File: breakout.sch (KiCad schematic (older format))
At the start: 16 parts, among them CON1 SD_Card, CON2 USB-MINI-B, P2 CONN_01X40, P3 CONN_01X40, P4 CONN_01X40, P5 A-DF-09-A/KG-T4S

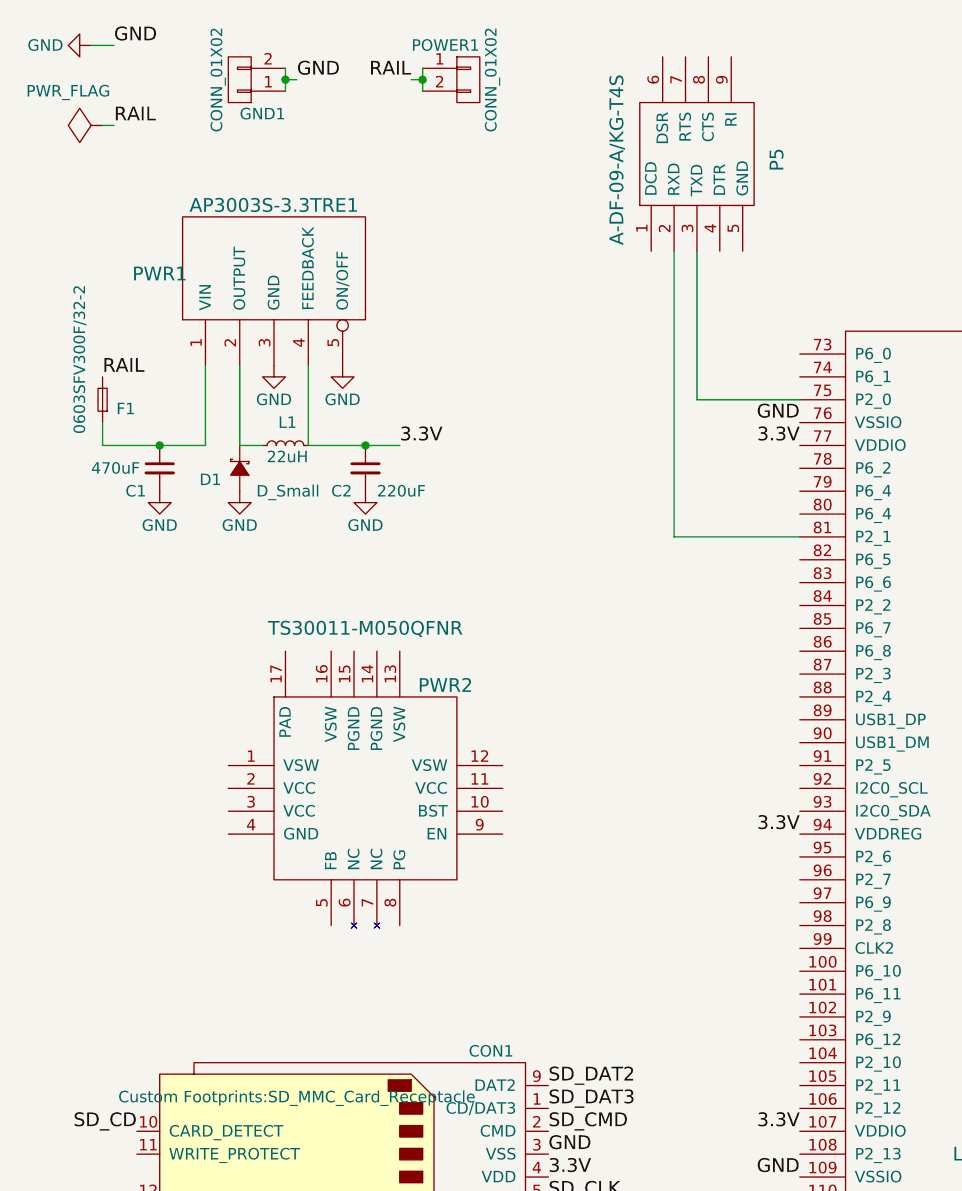
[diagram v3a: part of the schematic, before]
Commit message: added USB_MINI_AB_SMD footprint
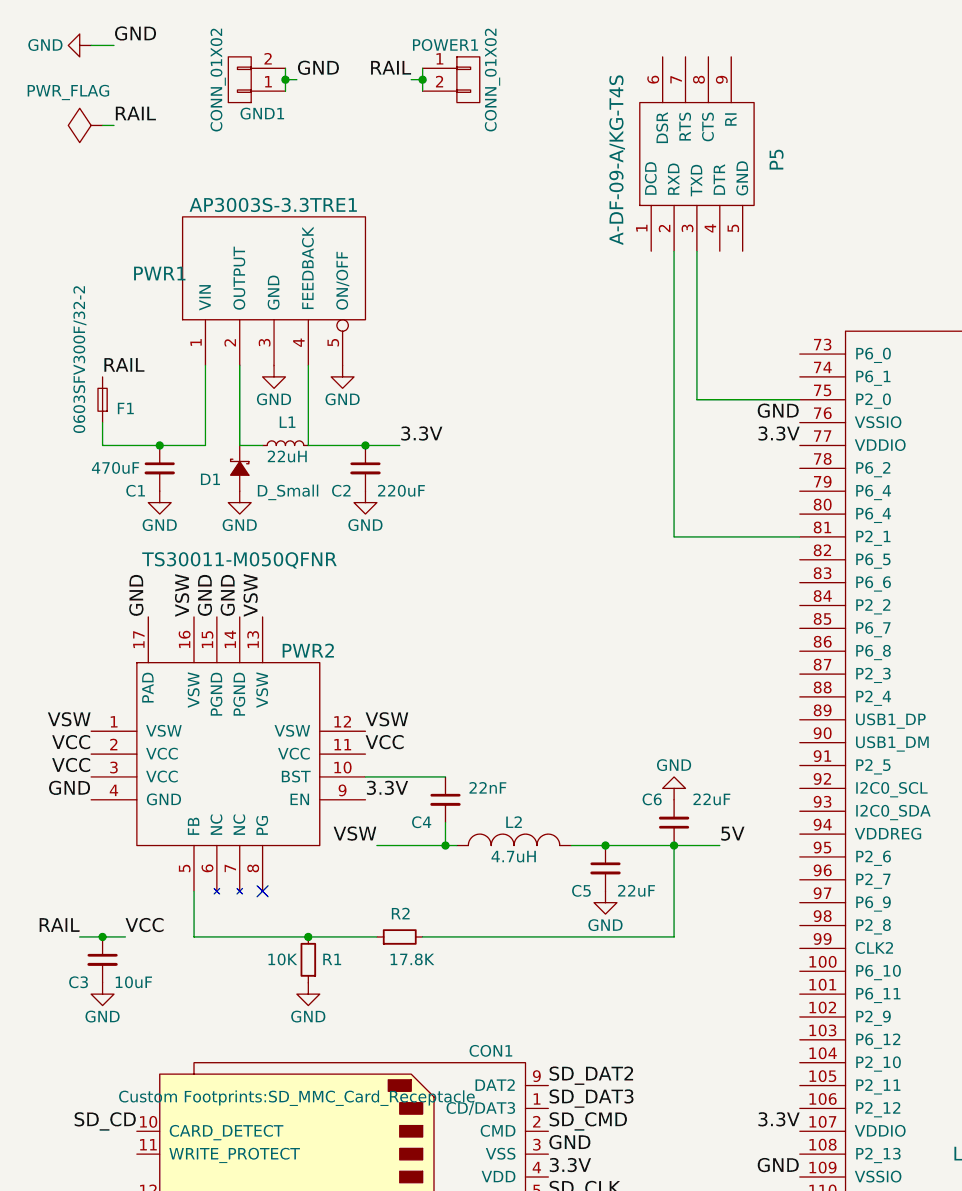
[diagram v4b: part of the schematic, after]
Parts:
- added C3: 10uF, Capacitors_SMD:C_0402, symbol C_Small
- added C4: 22nF, Capacitors_SMD:C_0402, symbol C_Small
- added C5, C6: 22uF, Capacitors_SMD:C_0402, symbol C_Small
- added L2: 4.7uH, Capacitors_SMD:C_0201, symbol INDUCTOR_SMALL
- added R1: 10K, Resistors_SMD:R_0201, symbol R_Small
- added R2: 17.8K, Resistors_SMD:R_0201, symbol R_Small
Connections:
- net 3.3V: now also PWR2.9 (EN); no longer CPU1.94 (VDDREG)
- net GND: now also PWR2.14 (PGND), PWR2.15 (PGND), PWR2.17 (PAD), PWR2.4 (GND), C3.2, C5.2, C6.2, R1.1
- net RAIL: now also PWR2.11 (VCC), PWR2.2 (VCC), PWR2.3 (VCC), C3.1
- net VSW: now reaches PWR2.1 (VSW)
- net VSW: now also PWR2.12 (VSW), PWR2.13 (VSW), PWR2.16 (VSW), C4.2, L2.1
- net at PWR2.10 (BST): now also C4.1
- net at PWR2.5 (FB): now also R1.2, R2.1
- new net 5V: C5.1, C6.1, L2.2, R2.2
- no-connect marks 0 -> 1
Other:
- moved on the sheet: PWR2
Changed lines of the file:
@@
 L TS30011-M050QFNR PWR2
 U 1 1 561BCBF8
-P 2000 3150
-F 0 "PWR2" H 2350 2900 60  0000 C CNN
-F 1 "TS30011-M050QFNR" H 2000 3150 60  0000 C CNN
-F 2 "Housings_DFN_QFN:QFN-16-1EP_3x3mm_Pitch0.5mm" H 2000 3150 60  0001 C CNN
-F 3 "" H 2000 3150 60  0000 C CNN
-	1    2000 3150
-	1    0    0    -1
-$EndComp
-$Comp
-L PWR_FLAG #FLG01
+P 1400 3000
+F 0 "PWR2" H 1750 2750 60  0000 C CNN
+F 1 "TS30011-M050QFNR" H 1450 3150 60  0000 C CNN
+F 2 "Housings_DFN_QFN:QFN-16-1EP_3x3mm_Pitch0.5mm" H 1400 3000 60  0001 C CNN
+F 3 "" H 1400 3000 60  0000 C CNN
+	1    1400 3000
+	1    0    0    -1
+$EndComp
+$Comp
+L PWR_FLAG #FLG1
 U 1 1 561BDFAD
 P 850 950
-F 0 "#FLG01" H 850 1045 50  0001 C CNN
+F 0 "#FLG1" H 850 1045 50  0001 C CNN
 F 1 "PWR_FLAG" V 1000 1100 50  0000 C CNN
 F 2 "" H 850 950 60  0000 C CNN
@@
 RAIL
 $Comp
-L GND #PWR02
+L GND #PWR1
 U 1 1 561BE928
 P 800 600
-F 0 "#PWR02" H 800 350 50  0001 C CNN
+F 0 "#PWR1" H 800 350 50  0001 C CNN
 F 1 "GND" V 800 400 50  0000 C CNN
 F 2 "" H 800 600 60  0000 C CNN
@@
 $EndComp
 $Comp
-L GND #PWR03
+L GND #PWR5
 U 1 1 561C5C16
 P 1600 2000
-F 0 "#PWR03" H 1600 1750 50  0001 C CNN
+F 0 "#PWR5" H 1600 1750 50  0001 C CNN
 F 1 "GND" H 1600 1850 50  0000 C CNN
 F 2 "" H 1600 2000 60  0000 C CNN
@@
 $EndComp
 $Comp
-L GND #PWR04
+L GND #PWR3
 U 1 1 561C5DB0
 P 1100 2550
-F 0 "#PWR04" H 1100 2300 50  0001 C CNN
+F 0 "#PWR3" H 1100 2300 50  0001 C CNN
 F 1 "GND" H 1100 2400 50  0000 C CNN
 F 2 "" H 1100 2550 60  0000 C CNN
@@
 $EndComp
 $Comp
-L GND #PWR05
+L GND #PWR7
 U 1 1 561C5E4C
 P 1900 2000
-F 0 "#PWR05" H 1900 1750 50  0001 C CNN
+F 0 "#PWR7" H 1900 1750 50  0001 C CNN
 F 1 "GND" H 1900 1850 50  0000 C CNN
 F 2 "" H 1900 2000 60  0000 C CNN
@@
 	1750 2000 1750 2350
 $Comp
-L GND #PWR06
+L GND #PWR4
 U 1 1 561C689A
 P 1450 2550
-F 0 "#PWR06" H 1450 2300 50  0001 C CNN
+F 0 "#PWR4" H 1450 2300 50  0001 C CNN
 F 1 "GND" H 1450 2400 50  0000 C CNN
 F 2 "" H 1450 2550 60  0000 C CNN
@@
 	1300 2350 1300 2000
 Wire Wire Line
-	850  2350 1100 2350
-Wire Wire Line
-	1100 2350 1300 2350
+	850  2350 1300 2350
 Wire Wire Line
 	850  2350 850  2250
 Wire Wire Line
-	1750 2350 2000 2350
-Wire Wire Line
-	2000 2350 2150 2350
+	1750 2350 2150 2350
 $Comp
 L C_Small C2
@@
 $EndComp
 $Comp
-L GND #PWR07
+L GND #PWR8
 U 1 1 561C6F20
 P 2000 2550
-F 0 "#PWR07" H 2000 2300 50  0001 C CNN
+F 0 "#PWR8" H 2000 2300 50  0001 C CNN
 F 1 "GND" H 2000 2400 50  0000 C CNN
 F 2 "" H 2000 2550 60  0000 C CNN
@@
 	850  950  900  950
 Wire Wire Line
-	1650 700  1650 750
-Wire Wire Line
-	1650 750  1650 800
+	1650 700  1650 800
 Wire Wire Line
 	1650 750  1700 750
@@
 GND
 Wire Wire Line
-	2250 700  2250 750
-Wire Wire Line
-	2250 750  2250 800
+	2250 700  2250 800
 Wire Wire Line
 	2250 750  2200 750
@@
 3.3V
 Text Label 3900 2350 2    60   ~ 0
-3.3V
-Text Label 3900 4050 2    60   ~ 0
 3.3V
 Text Label 3900 5350 2    60   ~ 0
@@
 Text Label 5900 3150 0    60   ~ 0
 SD_CD
+Text Label 800  3800 2    60   ~ 0
+VCC
+Text Label 800  3700 2    60   ~ 0
+VCC
+Text Label 2000 3700 0    60   ~ 0
+VCC
+Text Label 2000 3900 0    60   ~ 0
+3.3V
+Text Label 1050 3100 1    60   ~ 0
+GND
+Text Label 800  3900 2    60   ~ 0
+GND
+Text Label 1350 3100 1    60   ~ 0
+GND
+Text Label 1450 3100 1    60   ~ 0
+GND
+Text Label 1250 3100 1    60   ~ 0
+VSW
+Text Label 1550 3100 1    60   ~ 0
+VSW
+Text Label 2000 3600 0    60   ~ 0
+VSW
+Text Label 800  3600 2    60   ~ 0
+VSW
+Text Label 2050 4100 2    60   ~ 0
+VSW
+$Comp
+L INDUCTOR_SMALL L2
+U 1 1 561EBE7B
+P 2650 4100
+F 0 "L2" H 2650 4200 50  0000 C CNN
+F 1 "4.7uH" H 2650 4050 50  0000 C CNN
+F 2 "Capacitors_SMD:C_0201" H 2650 4100 60  0001 C CNN
+F 3 "" H 2650 4100 60  0000 C CNN
+	1    2650 4100
+	1    0    0    -1
+$EndComp
+$Comp
+L C_Small C5
+U 1 1 561ED0E2
+P 3050 4200
+F 0 "C5" H 2900 4100 50  0000 L CNN
+F 1 "22uF" H 3100 4100 50  0000 L CNN
+F 2 "Capacitors_SMD:C_0402" H 3050 4200 60  0001 C CNN
+F 3 "" H 3050 4200 60  0000 C CNN
+	1    3050 4200
+	1    0    0    -1
+$EndComp
+$Comp
+L C_Small C6
+U 1 1 561ED13D
+P 3350 4000
+F 0 "C6" H 3400 3900 50  0000 L CNN
+F 1 "22uF" H 3100 3900 50  0000 L CNN
+F 2 "Capacitors_SMD:C_0402" H 3350 4000 60  0001 C CNN
+F 3 "" H 3350 4000 60  0000 C CNN
+	1    3350 4000
+	-1   0    0    1
+$EndComp
+Wire Wire Line
+	2900 4100 3550 4100
+Connection ~ 3050 4100
+$Comp
+L GND #PWR9
+U 1 1 561ED8AD
+P 3050 4300
+F 0 "#PWR9" H 3050 4050 50  0001 C CNN
+F 1 "GND" H 3050 4150 50  0000 C CNN
+F 2 "" H 3050 4300 60  0000 C CNN
+F 3 "" H 3050 4300 60  0000 C CNN
+	1    3050 4300
+	1    0    0    -1
+$EndComp
+$Comp
+L GND #PWR10
+U 1 1 561ED8D4
+P 3350 3900
+F 0 "#PWR10" H 3350 3650 50  0001 C CNN
+F 1 "GND" H 3350 3750 50  0000 C CNN
+F 2 "" H 3350 3900 60  0000 C CNN
+F 3 "" H 3350 3900 60  0000 C CNN
+	1    3350 3900
+	-1   0    0    1
+$EndComp
+Text Label 3550 4100 0    60   ~ 0
+5V
+Connection ~ 3350 4100
+Wire Wire Line
+	2050 4100 2400 4100
+Wire Wire Line
+	2000 3800 2350 3800
+Wire Wire Line
+	1250 4300 1250 4500
+Wire Wire Line
+	3350 4500 3350 4100
+Text Label 750  4500 2    60   ~ 0
+RAIL
+Text Label 950  4500 0    60   ~ 0
+VCC
+Wire Wire Line
+	750  4500 950  4500
+$Comp
+L C_Small C3
+U 1 1 561F5813
+P 850 4600
+F 0 "C3" H 700 4500 50  0000 L CNN
+F 1 "10uF" H 900 4500 50  0000 L CNN
+F 2 "Capacitors_SMD:C_0402" H 850 4600 60  0001 C CNN
+F 3 "" H 850 4600 60  0000 C CNN
+	1    850  4600
+	1    0    0    -1
+$EndComp
+$Comp
+L GND #PWR2
+U 1 1 561F5842
+P 850 4700
+F 0 "#PWR2" H 850 4450 50  0001 C CNN
+F 1 "GND" H 850 4550 50  0000 C CNN
+F 2 "" H 850 4700 60  0000 C CNN
+F 3 "" H 850 4700 60  0000 C CNN
+	1    850  4700
+	1    0    0    -1
+$EndComp
+Connection ~ 850  4500
+$Comp
+L C_Small C4
+U 1 1 561F6598
+P 2350 3900
+F 0 "C4" H 2200 3800 50  0000 L CNN
+F 1 "22nF" H 2450 3950 50  0000 L CNN
+F 2 "Capacitors_SMD:C_0402" H 2350 3900 60  0001 C CNN
+F 3 "" H 2350 3900 60  0000 C CNN
+	1    2350 3900
+	1    0    0    -1
+$EndComp
+Wire Wire Line
+	2350 4000 2350 4100
+Connection ~ 2350 4100
+NoConn ~ 1550 4300
+$Comp
+L R_Small R2
+U 1 1 561F82A3
+P 2150 4500
+F 0 "R2" V 2250 4450 50  0000 L CNN
+F 1 "17.8K" V 2050 4350 50  0000 L CNN
+F 2 "Resistors_SMD:R_0201" H 2150 4500 60  0001 C CNN
+F 3 "" H 2150 4500 60  0000 C CNN
+	1    2150 4500
+	0    -1   -1   0
+$EndComp
+$Comp
+L R_Small R1
+U 1 1 561F8304
+P 1750 4600
+F 0 "R1" H 1600 4600 50  0000 L CNN
+F 1 "10K" H 1800 4600 50  0000 L CNN
+F 2 "Resistors_SMD:R_0201" H 1750 4600 60  0001 C CNN
+F 3 "" H 1750 4600 60  0000 C CNN
+	1    1750 4600
+	-1   0    0    1
+$EndComp
+Wire Wire Line
+	1250 4500 2050 4500
+Connection ~ 1750 4500
+Wire Wire Line
+	2250 4500 3350 4500
+$Comp
+L GND #PWR6
+U 1 1 561F854B
+P 1750 4700
+F 0 "#PWR6" H 1750 4450 50  0001 C CNN
+F 1 "GND" H 1750 4550 50  0000 C CNN
+F 2 "" H 1750 4700 60  0000 C CNN
+F 3 "" H 1750 4700 60  0000 C CNN
+	1    1750 4700
+	1    0    0    -1
+$EndComp
 $EndSCHEMATC

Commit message: syncing pcb layout with schematic
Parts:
- removed CON2: USB-MINI-B, Connect:USB_Mini-B, symbol USB-MINI-B
- added CON2: USB-MICRO-AB-SMD, Custom Footprints:USB_MICRO_AB, symbol USB-MICRO-AB-SMD
- added G1: 9007-05-00, Custom Footprints:9007-05-00, symbol 9007-05-00
- added R3, R4, R5: 10k, symbol R_Small
- added S1: 210-6MS, Buttons_Switches_ThroughHole:SW_DIP_x6_Slide, symbol 210-6MS
- added SW1: SW_PUSH, symbol SW_PUSH
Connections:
- net 3.3V: now also CPU1.94 (VDDREG), R4.2, R5.1
- net 5V: now also G1.1
- net GND: now also CON2.5 (GND), G1.3, R3.2, R5.2, S1.12, SW1.2
- net RESET: now reaches CPU1.128 (RESET)
- net RESET: now also SW1.1
- net at CPU1.18 (USB0_DP): now also CON2.3 (D+)
- net at CPU1.20 (USB0_DM): now also CON2.2 (D-)
- net at CPU1.22 (USB0_ID): now also CON2.4 (ID)
- net IC_WP: now reaches CPU1.32 (P0_0)
- net IC_WP: now also S1.11
- net USB0_IND0: now reaches CPU1.47 (P1_4)
- net at CPU1.75 (P2_0): now also P5.2 (RXD); no longer P5.3 (TXD)
- net at CPU1.81 (P2_1): now also P5.3 (TXD); no longer P5.2 (RXD)
- net USB0_PPWR: now reaches CPU1.87 (P2_3)
- net USB0_PPWR: now also G1.2, R3.1
- net ISP_ENABLE: now reaches CPU1.96 (P2_7)
- net ISP_ENABLE: now also R4.1, S1.1
- net SD_WP: now reaches CON1.11 (WRITE_PROTECT)
- net SD_WP: now also S1.2
- new net: CON2.1 (VBUS), G1.4
- no-connect marks 1 -> 5

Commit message: added boot select pins
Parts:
- added R6, R7, R8, R9: 10k, symbol R_Small
- F1: symbol F_Small -> FUSE_SMD
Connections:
- net 3.3V: now also R6.2, R7.2, R8.2, R9.2
- net GND: now also P5.5 (GND), S1.10, S1.7, S1.8, S1.9; no longer R5.2
- net RAIL: now also F1.1; no longer F1.2
- net RESET: now also R5.2
- net P2_9: now reaches CPU1.102 (P2_9)
- net P2_9: now also S1.6, R6.1
- net P1_1: now reaches CPU1.42 (P1_1)
- net P1_1: now also S1.3, R9.1
- net P1_2: now reaches CPU1.43 (P1_2)
- net P1_2: now also S1.4, R8.1
- net P2_8: now reaches CPU1.98 (P2_8)
- net P2_8: now also S1.5, R7.1
- net at C1.1, PWR1.1 (VIN): now also F1.2; no longer F1.1
- no-connect marks 5 -> 11
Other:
- moved on the sheet: R4, R5, S1, SW1

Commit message: fixed some more components
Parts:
- CON2: value USB-MICRO-AB-SMD -> USB-MICRO-AB; symbol USB-MICRO-AB-SMD -> USB-MICRO-AB
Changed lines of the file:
@@
 $EndComp
 $Comp
-L USB-MICRO-AB-SMD CON2
+L USB-MICRO-AB CON2
 U 1 1 561FF096
 P 7250 7050
 F 0 "CON2" H 7750 6950 60  0000 C CNN
-F 1 "USB-MICRO-AB-SMD" H 7450 6750 60  0000 C CNN
+F 1 "USB-MICRO-AB" H 7450 6750 60  0000 C CNN
 F 2 "Custom Footprints:USB_MICRO_AB" H 7250 7050 60  0001 C CNN
 F 3 "" H 7250 7050 60  0000 C CNN
@@
 F 0 "R4" H 2150 6750 50  0000 L CNN
 F 1 "10k" H 2100 6650 50  0000 L CNN
-F 2 "" H 2300 6700 60  0000 C CNN
+F 2 "" H 2300 6700 60  0001 C CNN
 F 3 "" H 2300 6700 60  0000 C CNN
 	1    2300 6700
@@
 F 0 "R5" H 980 8020 50  0000 L CNN
 F 1 "10k" H 980 7960 50  0000 L CNN
-F 2 "" H 950 8000 60  0000 C CNN
+F 2 "" H 950 8000 60  0001 C CNN
 F 3 "" H 950 8000 60  0000 C CNN
 	1    950  8000
@@
 F 0 "SW1" H 1400 8360 50  0000 C CNN
 F 1 "SW_PUSH" H 1250 8170 50  0000 C CNN
-F 2 "" H 1250 8250 60  0000 C CNN
+F 2 "" H 1250 8250 60  0001 C CNN
 F 3 "" H 1250 8250 60  0000 C CNN
 	1    1250 8250
@@
 F 0 "R9" H 1700 6750 50  0000 L CNN
 F 1 "10k" H 1650 6650 50  0000 L CNN
-F 2 "" H 1850 6700 60  0000 C CNN
+F 2 "" H 1850 6700 60  0001 C CNN
 F 3 "" H 1850 6700 60  0000 C CNN
 	1    1850 6700
@@
 F 0 "R8" H 1350 6750 50  0000 L CNN
 F 1 "10k" H 1300 6650 50  0000 L CNN
-F 2 "" H 1500 6700 60  0000 C CNN
+F 2 "" H 1500 6700 60  0001 C CNN
 F 3 "" H 1500 6700 60  0000 C CNN
 	1    1500 6700
@@
 F 0 "R7" H 1000 6750 50  0000 L CNN
 F 1 "10k" H 950 6650 50  0000 L CNN
-F 2 "" H 1150 6700 60  0000 C CNN
+F 2 "" H 1150 6700 60  0001 C CNN
 F 3 "" H 1150 6700 60  0000 C CNN
 	1    1150 6700
@@
 F 0 "R6" H 650 6750 50  0000 L CNN
 F 1 "10k" H 600 6650 50  0000 L CNN
-F 2 "" H 800 6700 60  0000 C CNN
+F 2 "" H 800 6700 60  0001 C CNN
 F 3 "" H 800 6700 60  0000 C CNN
 	1    800  6700

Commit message: adding components to the schematic, and fixing footprints
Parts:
- C2: footprint Capacitors_SMD:C_0201 -> Capacitors_Tantalum_SMD:TantalC_SizeB_EIA-3528_Reflow
- C3: footprint Capacitors_SMD:C_0402 -> Capacitors_Tantalum_SMD:TantalC_SizeC_EIA-6032_Reflow
- R1, R2: footprint Resistors_SMD:R_0201 -> Resistors_SMD:R_0402
- R3, R4, R5, R6, R7, R8, R9: footprint (none) -> Resistors_SMD:R_0402
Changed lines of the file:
@@
 F 0 "C2" H 1850 2350 50  0000 L CNN
 F 1 "220uF" H 2050 2350 50  0000 L CNN
-F 2 "Capacitors_SMD:C_0201" H 2000 2450 60  0001 C CNN
+F 2 "Capacitors_Tantalum_SMD:TantalC_SizeB_EIA-3528_Reflow" H 2000 2450 60  0001 C CNN
 F 3 "" H 2000 2450 60  0000 C CNN
 	1    2000 2450
@@
 F 0 "C3" H 700 4500 50  0000 L CNN
 F 1 "10uF" H 900 4500 50  0000 L CNN
-F 2 "Capacitors_SMD:C_0402" H 850 4600 60  0001 C CNN
+F 2 "Capacitors_Tantalum_SMD:TantalC_SizeC_EIA-6032_Reflow" H 850 4600 60  0001 C CNN
 F 3 "" H 850 4600 60  0000 C CNN
 	1    850  4600
@@
 F 0 "R2" V 2250 4450 50  0000 L CNN
 F 1 "17.8K" V 2050 4350 50  0000 L CNN
-F 2 "Resistors_SMD:R_0201" H 2150 4500 60  0001 C CNN
+F 2 "Resistors_SMD:R_0402" H 2150 4500 60  0001 C CNN
 F 3 "" H 2150 4500 60  0000 C CNN
 	1    2150 4500
@@
 F 0 "R1" H 1600 4600 50  0000 L CNN
 F 1 "10K" H 1800 4600 50  0000 L CNN
-F 2 "Resistors_SMD:R_0201" H 1750 4600 60  0001 C CNN
+F 2 "Resistors_SMD:R_0402" H 1750 4600 60  0001 C CNN
 F 3 "" H 1750 4600 60  0000 C CNN
 	1    1750 4600
@@
 F 0 "R3" H 6980 7570 50  0000 L CNN
 F 1 "10k" H 6980 7510 50  0000 L CNN
-F 2 "" H 6950 7550 60  0001 C CNN
+F 2 "Resistors_SMD:R_0402" H 6950 7550 60  0001 C CNN
 F 3 "" H 6950 7550 60  0000 C CNN
 	1    6950 7550
@@
 F 0 "R4" H 2150 6750 50  0000 L CNN
 F 1 "10k" H 2100 6650 50  0000 L CNN
-F 2 "" H 2300 6700 60  0001 C CNN
+F 2 "Resistors_SMD:R_0402" H 2300 6700 60  0001 C CNN
 F 3 "" H 2300 6700 60  0000 C CNN
 	1    2300 6700
@@
 F 0 "R5" H 980 8020 50  0000 L CNN
 F 1 "10k" H 980 7960 50  0000 L CNN
-F 2 "" H 950 8000 60  0001 C CNN
+F 2 "Resistors_SMD:R_0402" H 950 8000 60  0001 C CNN
 F 3 "" H 950 8000 60  0000 C CNN
 	1    950  8000
@@
 F 0 "R9" H 1700 6750 50  0000 L CNN
 F 1 "10k" H 1650 6650 50  0000 L CNN
-F 2 "" H 1850 6700 60  0001 C CNN
+F 2 "Resistors_SMD:R_0402" H 1850 6700 60  0001 C CNN
 F 3 "" H 1850 6700 60  0000 C CNN
 	1    1850 6700
@@
 F 0 "R8" H 1350 6750 50  0000 L CNN
 F 1 "10k" H 1300 6650 50  0000 L CNN
-F 2 "" H 1500 6700 60  0001 C CNN
+F 2 "Resistors_SMD:R_0402" H 1500 6700 60  0001 C CNN
 F 3 "" H 1500 6700 60  0000 C CNN
 	1    1500 6700
@@
 F 0 "R7" H 1000 6750 50  0000 L CNN
 F 1 "10k" H 950 6650 50  0000 L CNN
-F 2 "" H 1150 6700 60  0001 C CNN
+F 2 "Resistors_SMD:R_0402" H 1150 6700 60  0001 C CNN
 F 3 "" H 1150 6700 60  0000 C CNN
 	1    1150 6700
@@
 F 0 "R6" H 650 6750 50  0000 L CNN
 F 1 "10k" H 600 6650 50  0000 L CNN
-F 2 "" H 800 6700 60  0001 C CNN
+F 2 "Resistors_SMD:R_0402" H 800 6700 60  0001 C CNN
 F 3 "" H 800 6700 60  0000 C CNN
 	1    800  6700
